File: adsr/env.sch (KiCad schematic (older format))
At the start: 19 parts, among them Q1 2N3904, Q2 2N3904, U1 LM13700, U2 TL074, U3 DG403, U4 DG403

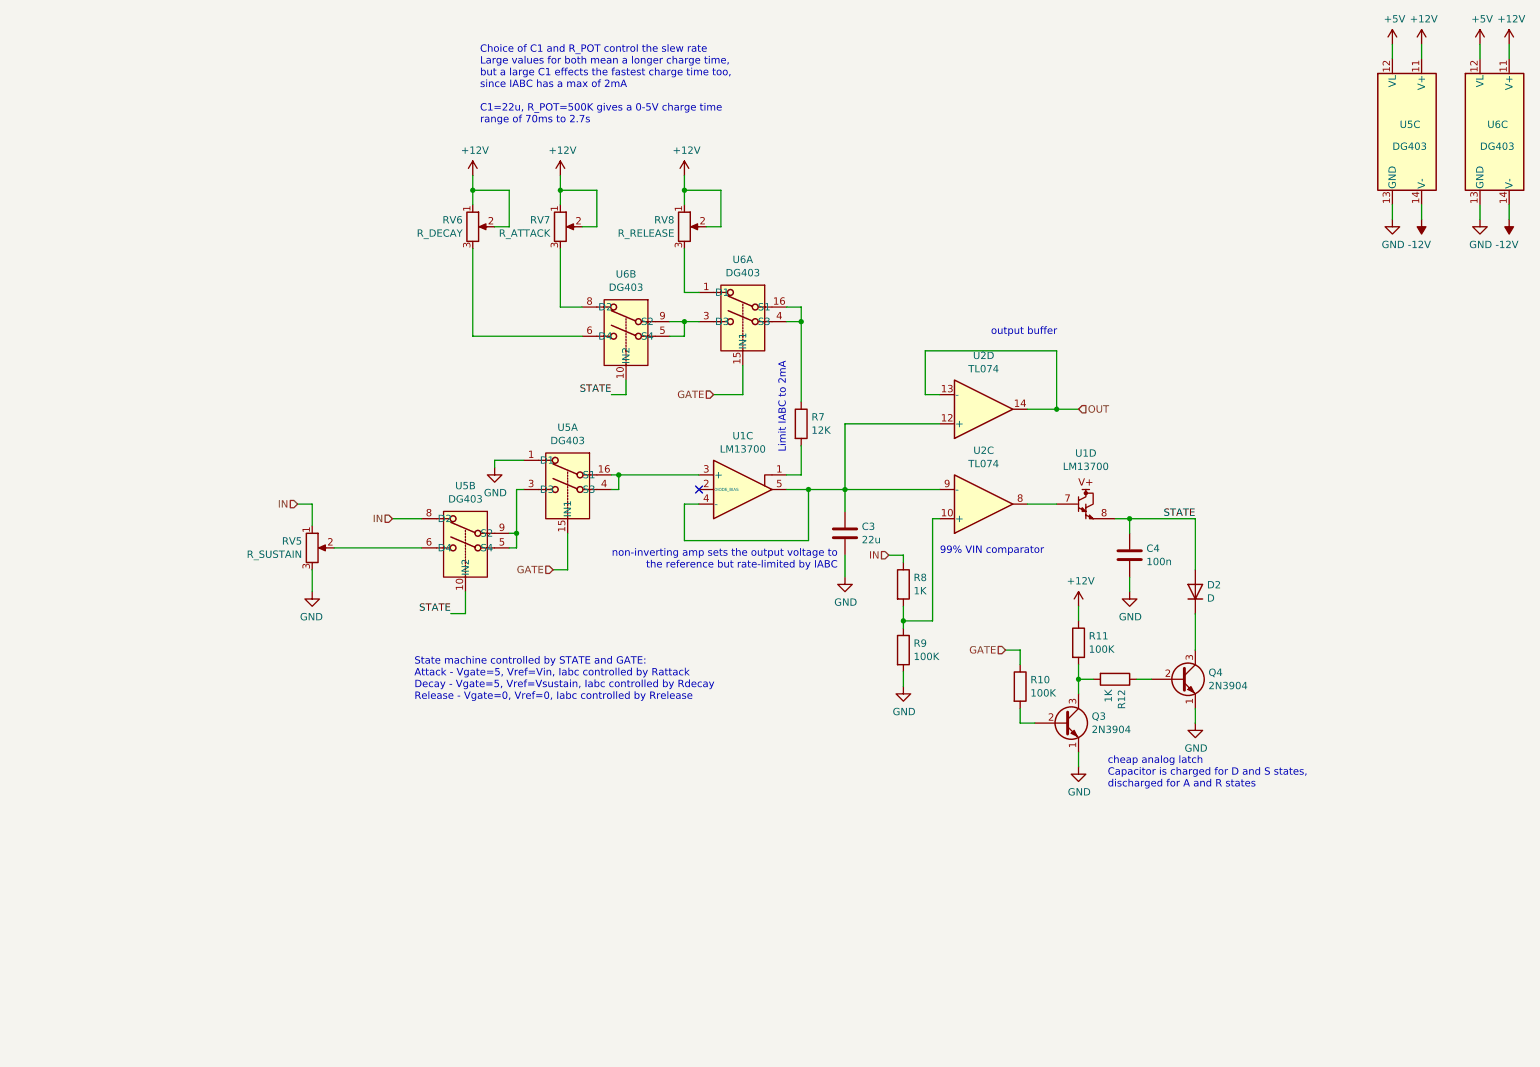
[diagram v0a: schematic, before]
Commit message: scaled adsr to support 0-10V input
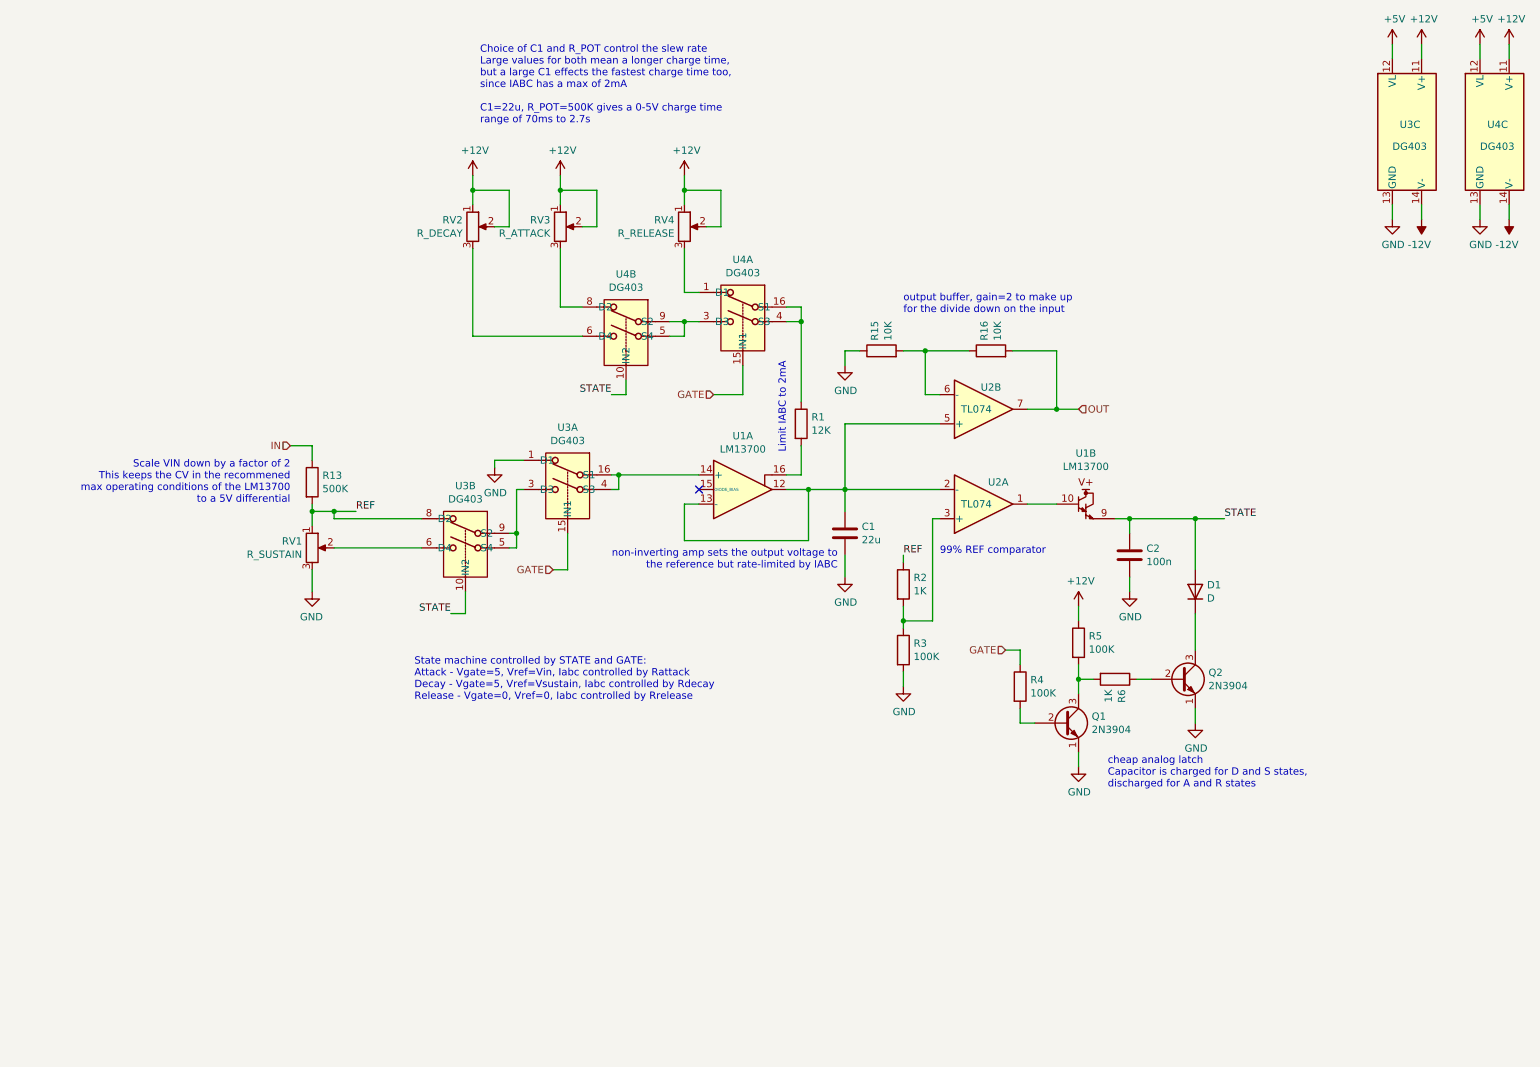
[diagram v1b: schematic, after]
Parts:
- added R13: 500K, Resistor_THT:R_Axial_DIN0204_L3.6mm_D1.6mm_P2.54mm_Vertical, symbol Device:R
- added R15, R16: 10K, Resistor_THT:R_Axial_DIN0204_L3.6mm_D1.6mm_P2.54mm_Vertical, symbol Device:R
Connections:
- net GND: now also R15.1
- net IN: now also R13.1; no longer R2.1, RV1.1, U3.8 (D2)
- net OUT: now also U2.7, R16.2; no longer U2.13 (-), U2.14
- net STATE: now also U1.9; no longer U1.8
- net at R1.2: now also U1.16; no longer U1.1
- net at U3.16 (S1), U3.4 (S3): now also U1.14 (+); no longer U1.3 (+)
- net at R2.2, R3.1: now also U2.3 (+); no longer U2.10 (+)
- new net: R15.2, R16.1, U2.6 (-)
- new net: C1.1, U1.12, U1.13 (-), U2.2 (-), U2.5 (+)
- new net: U1.10, U2.1
- new net REF: R13.2, R2.1, RV1.1, U3.8 (D2)
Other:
- note added: "99% REF comparator"
- note added: "Scale VIN down by a factor of 2\nThis keeps the CV in the recommened\nmax operating conditions of the LM13700\nto a 5V differential"
- note added: "output buffer, gain=2 to make up\nfor the divide down on the input"
- note removed: "99% VIN comparator"
- note removed: "output buffer"

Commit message: use a current mirror to isolate reference currents, buffer vin, tune params
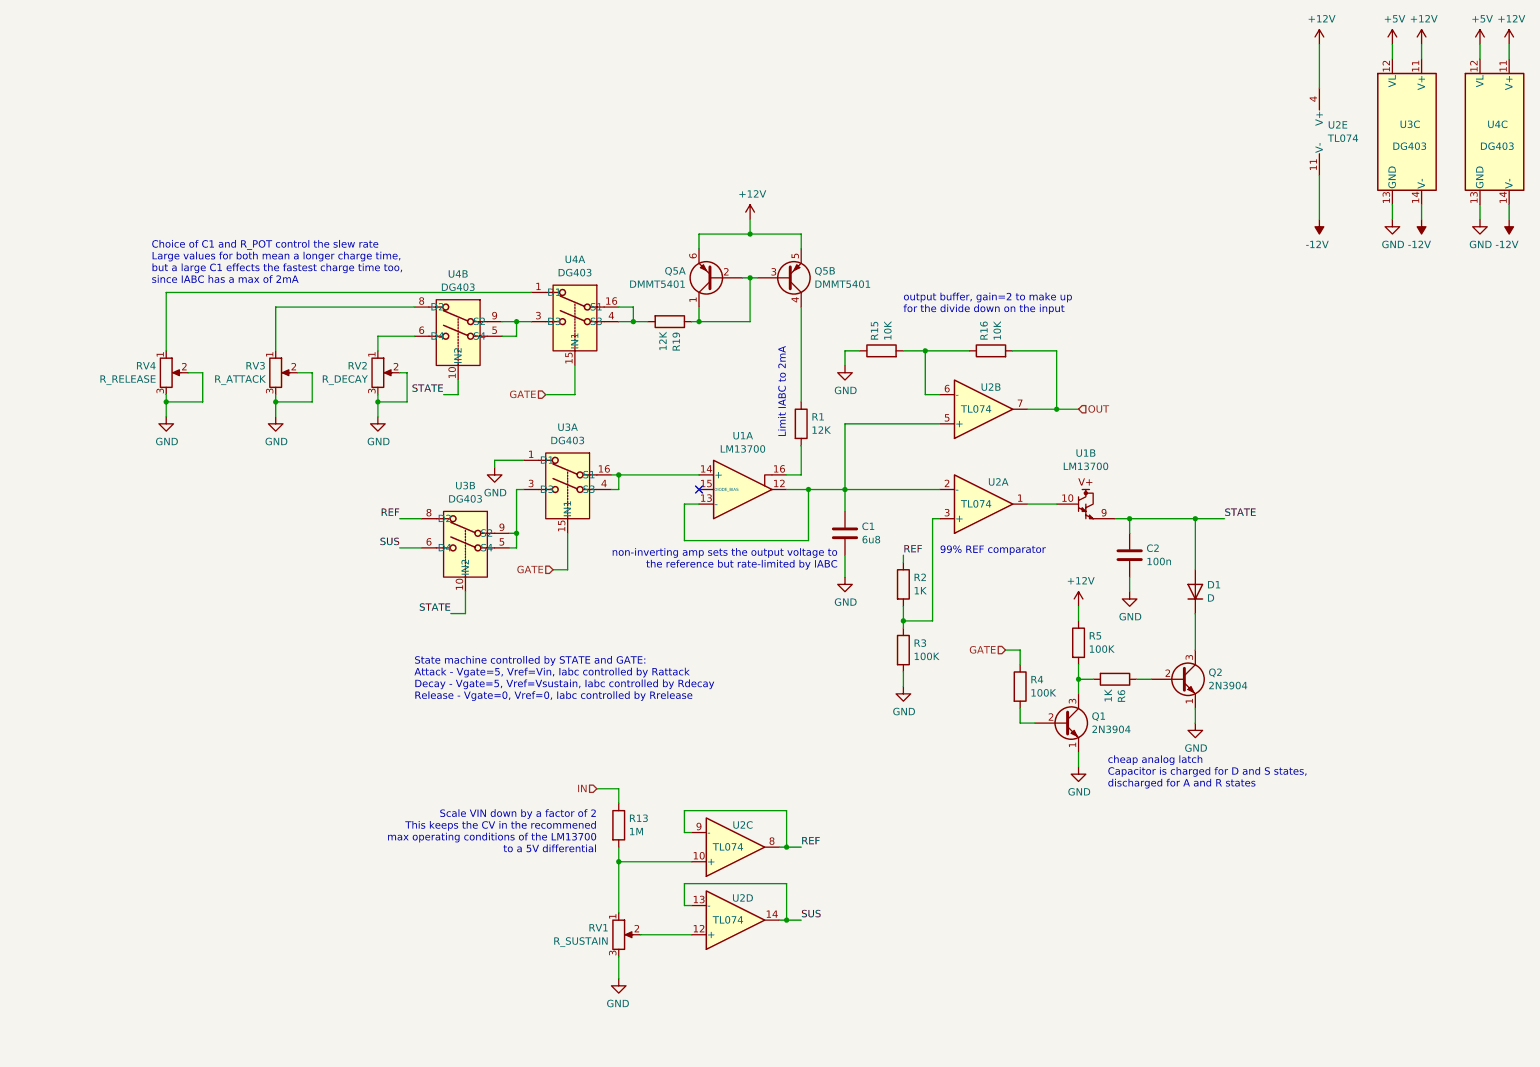
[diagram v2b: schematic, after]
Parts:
- added Q5: DMMT5401, KiCad/kicad-footprints/Package_TO_SOT_SMD.pretty:SOT-23-6, symbol synth:DMMT5401
- added R19: 12K, Resistor_THT:R_Axial_DIN0204_L3.6mm_D1.6mm_P2.54mm_Vertical, symbol Device:R
- added unit 3 of U2
- added unit 4 of U2
- added unit 5 of U2
- C1: value 22u -> 6u8
- R13: value 500K -> 1M
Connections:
- net +12V: now also Q5.5 (E2), Q5.6 (E1), U2.4 (V+); no longer RV2.1, RV2.2, RV3.1, RV3.2, RV4.1, RV4.2
- net -12V: now also U2.11 (V-)
- net GND: now also RV2.2, RV2.3, RV3.2, RV3.3, RV4.2, RV4.3
- net REF: now also U2.8, U2.9 (-); no longer R13.2, RV1.1
- net at U4.16 (S1), U4.4 (S3): now also R19.2; no longer R1.1
- net at RV1.2: now also U2.12 (+); no longer U3.6 (D4)
- net at U4.1 (D1): now also RV4.1; no longer RV4.3
- net at U4.6 (D4): now also RV2.1; no longer RV2.3
- net at U4.8 (D2): now also RV3.1; no longer RV3.3
- new net: R13.2, RV1.1, U2.10 (+)
- new net: Q5.1 (C1), Q5.2 (B1), Q5.3 (B2), R19.1
- new net: Q5.4 (C2), R1.1
- new net SUS: U2.13 (-), U2.14, U3.6 (D4)
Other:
- note added: "Choice of C1 and R_POT control the slew rate\nLarge values for both mean a longer charge time,\nbut a large C1 effects the fastest charge time too,\nsince IABC has a max of 2mA"
- note removed: "Choice of C1 and R_POT control the slew rate\nLarge values for both mean a longer charge time,\nbut a large C1 effects the fastest charge time too,\nsince IABC has a max of 2mA\n\nC1=22u, R_POT=500K gives a 0-5V charge time\nrange of 70ms to 2.7s"
- moved on the sheet: R13, RV1, RV2, RV3, RV4, U4A, U4B

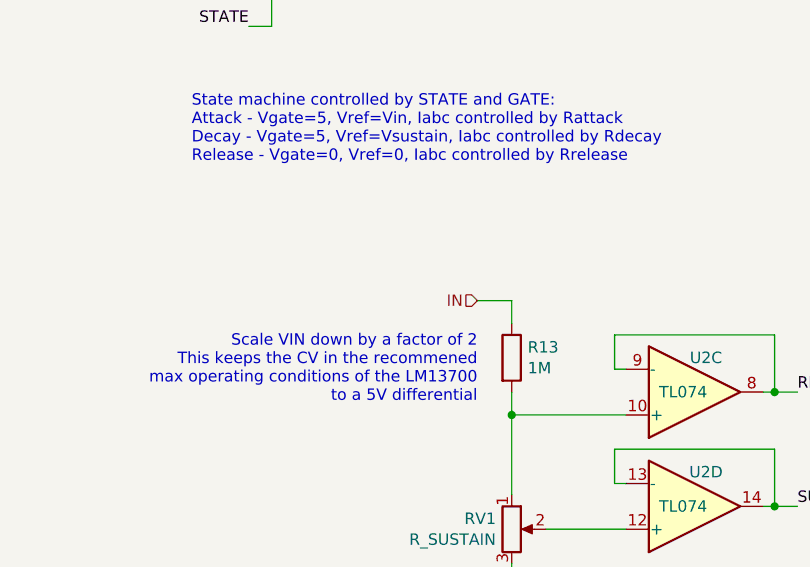
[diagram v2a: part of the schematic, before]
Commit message: use diode to force positive VIN
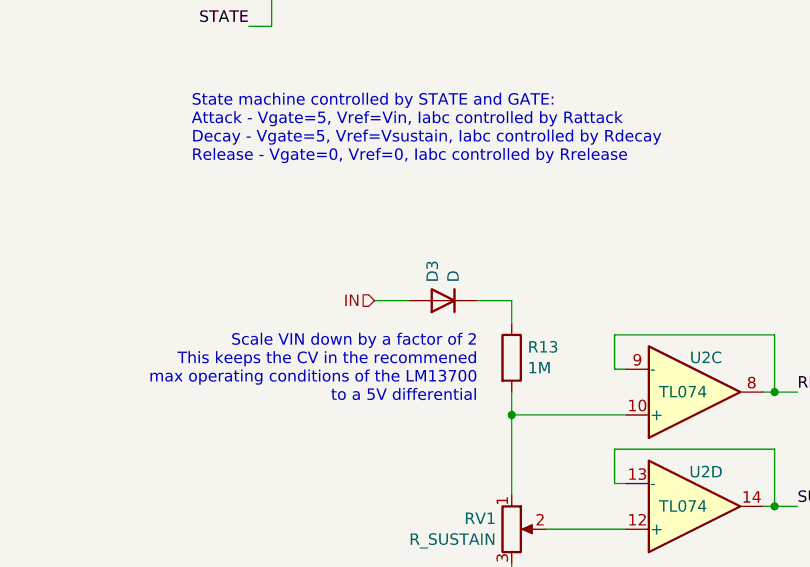
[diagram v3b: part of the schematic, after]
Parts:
- added D3: D, Diode_THT:D_A-405_P7.62mm_Horizontal, symbol Device:D
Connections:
- net IN: now also D3.2 (A); no longer R13.1
- new net: D3.1 (K), R13.1
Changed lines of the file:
@@
 Text Notes 1550 2450 0    50   ~ 0
 Choice of C1 and R_POT control the slew rate\nLarge values for both mean a longer charge time,\nbut a large C1 effects the fastest charge time too,\nsince IABC has a max of 2mA
-Text HLabel 4600 5900 0    50   Input ~ 0
+Text HLabel 4150 5900 0    50   Input ~ 0
 IN
 Text HLabel 4250 3200 0    50   Input ~ 0
@@
 Wire Wire Line
 	9550 2000 9550 1700
+$Comp
+L Device:D D?
+U 1 1 5F557E39
+P 4450 5900
+AR Path="/5F557E39" Ref="D?"  Part="1"
+AR Path="/5F5446F0/5F557E39" Ref="D3"  Part="1"
+AR Path="/5F5D80AF/5F557E39" Ref="D4"  Part="1"
+F 0 "D3" V 4496 5820 50  0000 R CNN
+F 1 "D" V 4405 5820 50  0000 R CNN
+F 2 "Diode_THT:D_A-405_P7.62mm_Horizontal" H 4450 5900 50  0001 C CNN
+F 3 "~" H 4450 5900 50  0001 C CNN
+	1    4450 5900
+	-1   0    0    1
+$EndComp
+Wire Wire Line
+	4150 5900 4300 5900
 $EndSCHEMATC

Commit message: rework ASDR
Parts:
- removed RV1: R_SUSTAIN, Connector_PinHeader_2.54mm:PinHeader_1x03_P2.54mm_Vertical, symbol Device:R_POT
- removed RV2: R_DECAY, Connector_PinHeader_2.54mm:PinHeader_1x03_P2.54mm_Vertical, symbol Device:R_POT
- removed RV3: R_ATTACK, Connector_PinHeader_2.54mm:PinHeader_1x03_P2.54mm_Vertical, symbol Device:R_POT
- removed RV4: R_RELEASE, Connector_PinHeader_2.54mm:PinHeader_1x03_P2.54mm_Vertical, symbol Device:R_POT
- added C7, C8: 0.1u, Capacitor_SMD:C_1206_3216Metric_Pad1.42x1.75mm_HandSolder, symbol Device:C
- added J10: Conn_01x08_Male, Connector_PinSocket_2.54mm:PinSocket_1x08_P2.54mm_Vertical, symbol Connector:Conn_01x08_Male
- added J9: Conn_01x08_Female, Connector_PinSocket_2.54mm:PinSocket_1x08_P2.54mm_Vertical, symbol Connector:Conn_01x08_Female
- added RV1: R_ATTACK, synth:Potentiometer_Alpha_RD902F-40-00D_Dual_Vertical, symbol Device:R_POT_Dual_Separate
- added RV2: R_DECAY, synth:Potentiometer_Alpha_RD902F-40-00D_Dual_Vertical, symbol Device:R_POT_Dual_Separate
- added RV3: R_SUSTAIN, synth:Potentiometer_Alpha_RD902F-40-00D_Dual_Vertical, symbol Device:R_POT_Dual_Separate
- added RV4: R_RELEASE, synth:Potentiometer_Alpha_RD902F-40-00D_Dual_Vertical, symbol Device:R_POT_Dual_Separate
- C1: value 6u8 -> 4.7u; footprint Resistor_THT:R_Axial_DIN0204_L3.6mm_D1.6mm_P2.54mm_Vertical -> Capacitor_SMD:C_1206_3216Metric_Pad1.42x1.75mm_HandSolder
- C2: footprint Capacitor_THT:C_Rect_L10.0mm_W2.5mm_P7.50mm_MKS4 -> Capacitor_SMD:C_1206_3216Metric_Pad1.42x1.75mm_HandSolder
- D1, D3: footprint Diode_THT:D_A-405_P7.62mm_Horizontal -> Diode_THT:D_A-405_P2.54mm_Vertical_AnodeUp
- Q5: footprint KiCad/kicad-footprints/Package_TO_SOT_SMD.pretty:SOT-23-6 -> Package_TO_SOT_SMD:SOT-23-6_Handsoldering
- R1, R19: value 12K -> 6.8k; footprint Resistor_THT:R_Axial_DIN0204_L3.6mm_D1.6mm_P2.54mm_Vertical -> Resistor_SMD:R_1206_3216Metric_Pad1.42x1.75mm_HandSolder
- R13, R15, R16, R2, R3, R4, R5, R6: footprint Resistor_THT:R_Axial_DIN0204_L3.6mm_D1.6mm_P2.54mm_Vertical -> Resistor_SMD:R_1206_3216Metric_Pad1.42x1.75mm_HandSolder
- U2: footprint (none) -> Package_DIP:DIP-14_W7.62mm
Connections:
- net +12V: now also C7.1
- net -12V: now also C8.2
- net GATE: now also J10.1 (Pin_1), J9.1 (Pin_1)
- net GND: now also C7.2, C8.1, J10.8 (Pin_8), J9.8 (Pin_8), RV1.5, RV1.6, RV2.5, RV2.6, RV3.4, RV4.5, RV4.6
- net OUT: now also J10.2 (Pin_2), J9.2 (Pin_2)
- net REF_RAW: now reaches R13.2, U2.10 (+)
- net REF_RAW: now also J10.5 (Pin_5), J9.5 (Pin_5), RV3.6
- net SUS_RAW: now reaches U2.12 (+)
- net SUS_RAW: now also J10.6 (Pin_6), J9.6 (Pin_6), RV3.5
- net RELEASE: now reaches U4.1 (D1)
- net RELEASE: now also J10.7 (Pin_7), J9.7 (Pin_7), RV4.4
- net DECAY: now reaches U4.6 (D4)
- net DECAY: now also J10.4 (Pin_4), J9.4 (Pin_4), RV2.4
- net ATTACK: now reaches U4.8 (D2)
- net ATTACK: now also J10.3 (Pin_3), J9.3 (Pin_3), RV1.4
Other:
- note added: "Cap IABC at 2mA"
- note added: "board interconnect"
- note added: "ceramic bypass capacitors for TL074\nclose to power supply pins"
- note removed: "Limit IABC to 2mA"
- moved on the sheet: C1

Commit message: more layout
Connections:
- net OUT: now also U2.14; no longer U2.7
- net REF: now also U2.1, U2.2 (-); no longer U2.8, U2.9 (-)
- net REF_RAW: now also U2.3 (+); no longer U2.10 (+)
- net SUS: now also U2.6 (-), U2.7; no longer U2.13 (-), U2.14
- net SUS_RAW: now also U2.5 (+); no longer U2.12 (+)
- net at R15.2, R16.1: now also U2.13 (-); no longer U2.6 (-)
- net at C1.1, U1.12, U1.13 (-): now also U2.12 (+), U2.9 (-); no longer U2.2 (-), U2.5 (+)
- net at U1.10: now also U2.8; no longer U2.1
- net at R2.2, R3.1: now also U2.10 (+); no longer U2.3 (+)
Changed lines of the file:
@@
 $Comp
 L Amplifier_Operational:TL074 U2
-U 1 1 5F585080
+U 3 1 5F585080
 P 7250 3950
-AR Path="/5F5446F0/5F585080" Ref="U2"  Part="1"
+AR Path="/5F5446F0/5F585080" Ref="U2"  Part="3"
 AR Path="/5F5D80AF/5F585080" Ref="U7"  Part="1"
 F 0 "U2" H 7350 3800 50  0000 C CNN
@@
 F 2 "Package_DIP:DIP-14_W7.62mm" H 7200 4050 50  0001 C CNN
 F 3 "http://www.ti.com/lit/ds/symlink/tl071.pdf" H 7300 4150 50  0001 C CNN
-	1    7250 3950
+	3    7250 3950
 	1    0    0    1
 $EndComp
 $Comp
 L Amplifier_Operational:TL074 U2
-U 2 1 5F585086
+U 4 1 5F585086
 P 7250 3300
-AR Path="/5F5446F0/5F585086" Ref="U2"  Part="2"
+AR Path="/5F5446F0/5F585086" Ref="U2"  Part="4"
 AR Path="/5F5D80AF/5F585086" Ref="U7"  Part="2"
 F 0 "U2" H 7300 3150 50  0000 C CNN
@@
 F 2 "Package_DIP:DIP-14_W7.62mm" H 7200 3400 50  0001 C CNN
 F 3 "http://www.ti.com/lit/ds/symlink/tl071.pdf" H 7300 3500 50  0001 C CNN
-	2    7250 3300
+	4    7250 3300
 	1    0    0    1
 $EndComp
@@
 $Comp
 L Amplifier_Operational:TL074 U2
-U 3 1 5F2911D2
+U 1 1 5F2911D2
 P 5550 6300
-AR Path="/5F5446F0/5F2911D2" Ref="U2"  Part="3"
+AR Path="/5F5446F0/5F2911D2" Ref="U2"  Part="1"
 AR Path="/5F5D80AF/5F2911D2" Ref="U7"  Part="3"
 F 0 "U2" H 5600 6150 50  0000 C CNN
@@
 F 2 "Package_DIP:DIP-14_W7.62mm" H 5500 6400 50  0001 C CNN
 F 3 "http://www.ti.com/lit/ds/symlink/tl071.pdf" H 5600 6500 50  0001 C CNN
-	3    5550 6300
+	1    5550 6300
 	1    0    0    1
 $EndComp
@@
 $Comp
 L Amplifier_Operational:TL074 U2
-U 4 1 5F2C52A2
+U 2 1 5F2C52A2
 P 5550 6800
-AR Path="/5F5446F0/5F2C52A2" Ref="U2"  Part="4"
+AR Path="/5F5446F0/5F2C52A2" Ref="U2"  Part="2"
 AR Path="/5F5D80AF/5F2C52A2" Ref="U7"  Part="4"
 F 0 "U2" H 5600 6650 50  0000 C CNN
@@
 F 2 "Package_DIP:DIP-14_W7.62mm" H 5500 6900 50  0001 C CNN
 F 3 "http://www.ti.com/lit/ds/symlink/tl071.pdf" H 5600 7000 50  0001 C CNN
-	4    5550 6800
+	2    5550 6800
 	1    0    0    1
 $EndComp
